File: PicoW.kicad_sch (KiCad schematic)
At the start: 1 part, among them U1 Pico

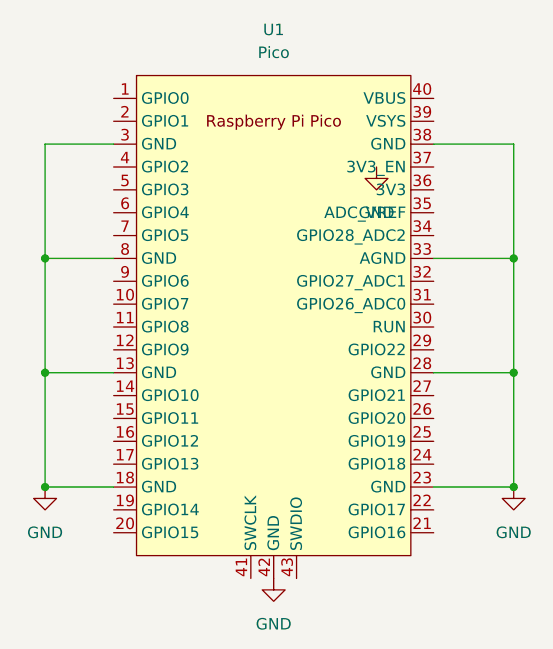
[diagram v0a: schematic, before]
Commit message: Adding pins for Pico
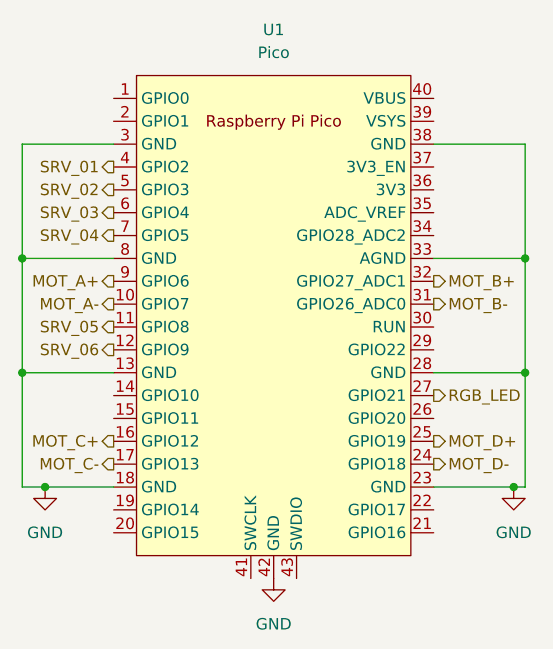
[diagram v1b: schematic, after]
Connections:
- net MOT_A-: now reaches U1.10 (GPIO7)
- net SRV_05: now reaches U1.11 (GPIO8)
- net SRV_06: now reaches U1.12 (GPIO9)
- net MOT_C+: now reaches U1.16 (GPIO12)
- net MOT_C-: now reaches U1.17 (GPIO13)
- net MOT_D-: now reaches U1.24 (GPIO18)
- net MOT_D+: now reaches U1.25 (GPIO19)
- net RGB_LED: now reaches U1.27 (GPIO21)
- net MOT_B-: now reaches U1.31 (GPIO26_ADC0)
- net MOT_B+: now reaches U1.32 (GPIO27_ADC1)
- net SRV_01: now reaches U1.4 (GPIO2)
- net SRV_02: now reaches U1.5 (GPIO3)
- net SRV_03: now reaches U1.6 (GPIO4)
- net SRV_04: now reaches U1.7 (GPIO5)
- net MOT_A+: now reaches U1.9 (GPIO6)
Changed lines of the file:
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@@
 (kicad_sch (version 20230121) (generator eeschema)
   (paper "A4")
+  (junction (at 170.18 97.79) (diameter 0) (color 0 0 0 0)
+  )
+  (junction (at 114.3 85.09) (diameter 0) (color 0 0 0 0)
+  )
+  (junction (at 170.18 85.09) (diameter 0) (color 0 0 0 0)
+  )
   (junction (at 168.91 110.49) (diameter 0) (color 0 0 0 0)
   )
-  (junction (at 168.91 85.09) (diameter 0) (color 0 0 0 0)
-  )
-  (junction (at 116.84 85.09) (diameter 0) (color 0 0 0 0)
-  )
-  (junction (at 168.91 97.79) (diameter 0) (color 0 0 0 0)
+  (junction (at 114.3 97.79) (diameter 0) (color 0 0 0 0)
   )
   (junction (at 116.84 110.49) (diameter 0) (color 0 0 0 0)
   )
-  (junction (at 116.84 97.79) (diameter 0) (color 0 0 0 0)
-  )
-  (wire (pts (xy 168.91 97.79) (xy 168.91 110.49))
+  (wire (pts (xy 170.18 97.79) (xy 170.18 110.49))
     (stroke (width 0) (type default))
   )
-  (wire (pts (xy 168.91 72.39) (xy 168.91 85.09))
+  (wire (pts (xy 114.3 97.79) (xy 124.46 97.79))
     (stroke (width 0) (type default))
   )
-  (wire (pts (xy 160.02 72.39) (xy 168.91 72.39))
+  (wire (pts (xy 170.18 72.39) (xy 170.18 85.09))
     (stroke (width 0) (type default))
   )
-  (wire (pts (xy 160.02 85.09) (xy 168.91 85.09))
+  (wire (pts (xy 114.3 72.39) (xy 114.3 85.09))
     (stroke (width 0) (type default))
   )
-  (wire (pts (xy 116.84 72.39) (xy 116.84 85.09))
+  (wire (pts (xy 160.02 72.39) (xy 170.18 72.39))
     (stroke (width 0) (type default))
   )
@@
     (stroke (width 0) (type default))
   )
-  (wire (pts (xy 116.84 97.79) (xy 124.46 97.79))
+  (wire (pts (xy 114.3 110.49) (xy 116.84 110.49))
     (stroke (width 0) (type default))
   )
-  (wire (pts (xy 160.02 97.79) (xy 168.91 97.79))
+  (wire (pts (xy 160.02 85.09) (xy 170.18 85.09))
+    (stroke (width 0) (type default))
+  )
+  (wire (pts (xy 160.02 97.79) (xy 170.18 97.79))
     (stroke (width 0) (type default))
   )
@@
     (stroke (width 0) (type default))
   )
-  (wire (pts (xy 116.84 97.79) (xy 116.84 110.49))
+  (wire (pts (xy 114.3 97.79) (xy 114.3 110.49))
     (stroke (width 0) (type default))
   )
-  (wire (pts (xy 116.84 85.09) (xy 116.84 97.79))
+  (wire (pts (xy 170.18 110.49) (xy 168.91 110.49))
     (stroke (width 0) (type default))
   )
-  (wire (pts (xy 168.91 85.09) (xy 168.91 97.79))
+  (wire (pts (xy 114.3 85.09) (xy 114.3 97.79))
     (stroke (width 0) (type default))
   )
-  (wire (pts (xy 124.46 72.39) (xy 116.84 72.39))
+  (wire (pts (xy 170.18 85.09) (xy 170.18 97.79))
     (stroke (width 0) (type default))
   )
-  (wire (pts (xy 116.84 85.09) (xy 124.46 85.09))
+  (wire (pts (xy 124.46 72.39) (xy 114.3 72.39))
     (stroke (width 0) (type default))
   )
-  (symbol (lib_id "power:GND") (at 153.67 74.93 0) (unit 1)
-    (in_bom yes) (on_board yes) (dnp no) (fields_autoplaced)
-    (property "Reference" "#PWR016" (at 153.67 81.28 0)
-      (effects (font (size 1.27 1.27)) hide)
-    )
-    (property "Value" "GND" (at 153.67 80.01 0)
-      (effects (font (size 1.27 1.27)))
-    )
-    (property "Footprint" "" (at 153.67 74.93 0)
-      (effects (font (size 1.27 1.27)) hide)
-    )
-    (property "Datasheet" "" (at 153.67 74.93 0)
-      (effects (font (size 1.27 1.27)) hide)
-    )
-    (pin "1")
-    (instances
-      (project "Pico-Skidi"
-        (path "/21865b85-eb74-4d61-a31a-30858d3bc341"
-          (reference "#PWR016") (unit 1)
-        )
-        (path "/21865b85-eb74-4d61-a31a-30858d3bc341/60530e3c-b075-4fd7-83a5-48bc65381cc4"
-          (reference "#PWR010") (unit 1)
-        )
-      )
-    )
+  (wire (pts (xy 114.3 85.09) (xy 124.46 85.09))
+    (stroke (width 0) (type default))
+  )
+  (hierarchical_label "MOT_A+" (shape output) (at 124.46 87.63 180) (fields_autoplaced)
+    (effects (font (size 1.27 1.27)) (justify right))
+  )
+  (hierarchical_label "MOT_A-" (shape output) (at 124.46 90.17 180) (fields_autoplaced)
+    (effects (font (size 1.27 1.27)) (justify right))
+  )
+  (hierarchical_label "SRV_01" (shape output) (at 124.46 74.93 180) (fields_autoplaced)
+    (effects (font (size 1.27 1.27)) (justify right))
+  )
+  (hierarchical_label "SRV_02" (shape output) (at 124.46 77.47 180) (fields_autoplaced)
+    (effects (font (size 1.27 1.27)) (justify right))
+  )
+  (hierarchical_label "SRV_03" (shape output) (at 124.46 80.01 180) (fields_autoplaced)
+    (effects (font (size 1.27 1.27)) (justify right))
+  )
+  (hierarchical_label "MOT_D+" (shape output) (at 160.02 105.41 0) (fields_autoplaced)
+    (effects (font (size 1.27 1.27)) (justify left))
+  )
+  (hierarchical_label "MOT_B-" (shape output) (at 160.02 90.17 0) (fields_autoplaced)
+    (effects (font (size 1.27 1.27)) (justify left))
+  )
+  (hierarchical_label "MOT_C+" (shape output) (at 124.46 105.41 180) (fields_autoplaced)
+    (effects (font (size 1.27 1.27)) (justify right))
+  )
+  (hierarchical_label "MOT_D-" (shape output) (at 160.02 107.95 0) (fields_autoplaced)
+    (effects (font (size 1.27 1.27)) (justify left))
+  )
+  (hierarchical_label "MOT_B+" (shape output) (at 160.02 87.63 0) (fields_autoplaced)
+    (effects (font (size 1.27 1.27)) (justify left))
+  )
+  (hierarchical_label "SRV_04" (shape output) (at 124.46 82.55 180) (fields_autoplaced)
+    (effects (font (size 1.27 1.27)) (justify right))
+  )
+  (hierarchical_label "SRV_06" (shape output) (at 124.46 95.25 180) (fields_autoplaced)
+    (effects (font (size 1.27 1.27)) (justify right))
+  )
+  (hierarchical_label "MOT_C-" (shape output) (at 124.46 107.95 180) (fields_autoplaced)
+    (effects (font (size 1.27 1.27)) (justify right))
+  )
+  (hierarchical_label "SRV_05" (shape output) (at 124.46 92.71 180) (fields_autoplaced)
+    (effects (font (size 1.27 1.27)) (justify right))
+  )
+  (hierarchical_label "RGB_LED" (shape output) (at 160.02 100.33 0) (fields_autoplaced)
+    (effects (font (size 1.27 1.27)) (justify left))
   )
   (symbol (lib_id "MCU_RaspberryPi_and_Boards:Pico") (at 142.24 91.44 0) (unit 1)
@@
         )
         (path "/21865b85-eb74-4d61-a31a-30858d3bc341/60530e3c-b075-4fd7-83a5-48bc65381cc4"
-          (reference "U1") (unit 1)
+          (reference "U?") (unit 1)
         )
       )

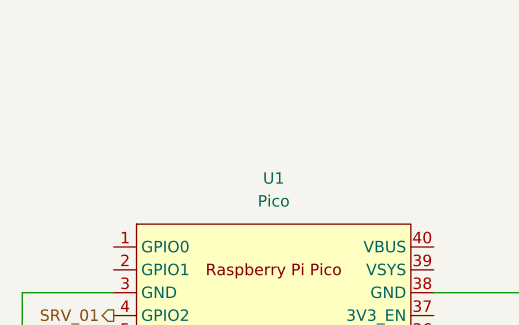
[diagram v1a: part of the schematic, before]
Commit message: Additional sheets in the schematic
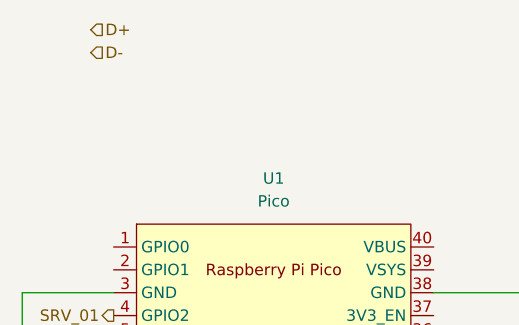
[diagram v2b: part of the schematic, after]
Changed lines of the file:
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@@
+    (effects (font (size 1.27 1.27)) (justify left))
+  )
+  (hierarchical_label "D-" (shape input) (at 121.92 45.72 0) (fields_autoplaced)
     (effects (font (size 1.27 1.27)) (justify left))
   )
@@
     (effects (font (size 1.27 1.27)) (justify right))
   )
+  (hierarchical_label "D+" (shape input) (at 121.92 43.18 0) (fields_autoplaced)
+    (effects (font (size 1.27 1.27)) (justify left))
+  )
   (hierarchical_label "RGB_LED" (shape output) (at 160.02 100.33 0) (fields_autoplaced)

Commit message: Lots of changes
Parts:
- added J7: Conn_01x03, Connector_PinHeader_2.54mm:PinHeader_1x03_P2.54mm_Vertical, symbol Connector_Generic:Conn_01x03
- added J8: Conn_01x04, Connector_PinHeader_2.54mm:PinHeader_1x04_P2.54mm_Vertical, symbol Connector_Generic:Conn_01x04
- U1: footprint RPi_Pico:RPi_Pico_SMD_TH -> MCU_RaspberryPi_and_Boards:RPi_Pico_W_SMD_TH
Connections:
- net GND: now also U1.44 (GND), J7.2 (Pin_2), J8.1 (Pin_1)
- net nFAULT_01: now reaches U1.14 (GPIO10)
- net nFAULT_02: now reaches U1.15 (GPIO11)
- net BUZZER: now reaches U1.19 (GPIO14)
- net SDA: now reaches U1.21 (GPIO16)
- net SDA: now also J8.3 (Pin_3)
- net SCL: now reaches U1.22 (GPIO17)
- net SCL: now also J8.4 (Pin_4)
- net +3.3V: now reaches U1.36 (3V3)
- net +3.3V: now also J8.2 (Pin_2)
- net +5V: now reaches U1.39 (VSYS)
- net VBUS: now reaches U1.40 (VBUS)
- net at U1.41 (SWCLK): now also J7.3 (Pin_3)
- net at U1.43 (SWDIO): now also J7.1 (Pin_1)
- new net BOOTSEL: U1.49 (BOOTSEL)
- new net USB_D+: U1.45 (D+)
- new net USB_D-: U1.46 (D-)
- no-connect marks 0 -> 9

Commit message: syncing
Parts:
- U1: footprint MCU_RaspberryPi_and_Boards:RPi_Pico_W_SMD_TH -> MCU_RaspberryPi_and_Boards:RPi_Pico_W_SMD
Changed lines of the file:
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@@
   (symbol (lib_id "power:+5V") (at 171.45 69.85 0) (unit 1)
     (in_bom yes) (on_board yes) (dnp no) (fields_autoplaced)
-    (property "Reference" "#PWR030" (at 171.45 73.66 0)
+    (property "Reference" "#PWR039" (at 171.45 73.66 0)
       (effects (font (size 1.27 1.27)) hide)
     )
@@
       (project "Pico-Skidi"
         (path "/21865b85-eb74-4d61-a31a-30858d3bc341/60530e3c-b075-4fd7-83a5-48bc65381cc4"
-          (reference "#PWR030") (unit 1)
+          (reference "#PWR039") (unit 1)
         )
       )
@@
   (symbol (lib_id "power:+3.3V") (at 187.96 68.58 0) (unit 1)
     (in_bom yes) (on_board yes) (dnp no) (fields_autoplaced)
-    (property "Reference" "#PWR031" (at 187.96 72.39 0)
+    (property "Reference" "#PWR040" (at 187.96 72.39 0)
       (effects (font (size 1.27 1.27)) hide)
     )
@@
       (project "Pico-Skidi"
         (path "/21865b85-eb74-4d61-a31a-30858d3bc341/60530e3c-b075-4fd7-83a5-48bc65381cc4"
-          (reference "#PWR031") (unit 1)
+          (reference "#PWR040") (unit 1)
         )
       )
@@
   (symbol (lib_id "power:VBUS") (at 165.1 67.31 0) (unit 1)
     (in_bom yes) (on_board yes) (dnp no) (fields_autoplaced)
-    (property "Reference" "#PWR027" (at 165.1 71.12 0)
+    (property "Reference" "#PWR036" (at 165.1 71.12 0)
       (effects (font (size 1.27 1.27)) hide)
     )
@@
       (project "Pico-Skidi"
         (path "/21865b85-eb74-4d61-a31a-30858d3bc341/60530e3c-b075-4fd7-83a5-48bc65381cc4"
-          (reference "#PWR027") (unit 1)
+          (reference "#PWR036") (unit 1)
         )
       )
@@
   (symbol (lib_id "power:+3.3V") (at 166.37 78.74 0) (unit 1)
     (in_bom yes) (on_board yes) (dnp no) (fields_autoplaced)
-    (property "Reference" "#PWR028" (at 166.37 82.55 0)
+    (property "Reference" "#PWR037" (at 166.37 82.55 0)
       (effects (font (size 1.27 1.27)) hide)
     )
@@
       (project "Pico-Skidi"
         (path "/21865b85-eb74-4d61-a31a-30858d3bc341/60530e3c-b075-4fd7-83a5-48bc65381cc4"
-          (reference "#PWR028") (unit 1)
+          (reference "#PWR037") (unit 1)
         )
       )
@@
       (effects (font (size 1.27 1.27)))
     )
-    (property "Footprint" "MCU_RaspberryPi_and_Boards:RPi_Pico_W_SMD_TH" (at 142.24 91.44 90)
+    (property "Footprint" "MCU_RaspberryPi_and_Boards:RPi_Pico_W_SMD" (at 142.24 91.44 90)
       (effects (font (size 1.27 1.27)) hide)
     )
@@
         )
         (path "/21865b85-eb74-4d61-a31a-30858d3bc341/60530e3c-b075-4fd7-83a5-48bc65381cc4"
-          (reference "U4") (unit 1)
+          (reference "U5") (unit 1)
         )
       )
@@
   (symbol (lib_id "power:GND") (at 193.04 62.23 0) (unit 1)
     (in_bom yes) (on_board yes) (dnp no) (fields_autoplaced)
-    (property "Reference" "#PWR032" (at 193.04 68.58 0)
+    (property "Reference" "#PWR041" (at 193.04 68.58 0)
       (effects (font (size 1.27 1.27)) hide)
     )
@@
       (project "Pico-Skidi"
         (path "/21865b85-eb74-4d61-a31a-30858d3bc341/60530e3c-b075-4fd7-83a5-48bc65381cc4"
-          (reference "#PWR032") (unit 1)
+          (reference "#PWR041") (unit 1)
         )
       )
@@
         )
         (path "/21865b85-eb74-4d61-a31a-30858d3bc341/60530e3c-b075-4fd7-83a5-48bc65381cc4"
-          (reference "#PWR029") (unit 1)
+          (reference "#PWR038") (unit 1)
         )
       )
@@
   (symbol (lib_id "power:GND") (at 142.24 128.27 0) (unit 1)
     (in_bom yes) (on_board yes) (dnp no) (fields_autoplaced)
-    (property "Reference" "#PWR026" (at 142.24 134.62 0)
+    (property "Reference" "#PWR035" (at 142.24 134.62 0)
       (effects (font (size 1.27 1.27)) hide)
     )
@@
       (project "Pico-Skidi"
         (path "/21865b85-eb74-4d61-a31a-30858d3bc341/60530e3c-b075-4fd7-83a5-48bc65381cc4"
-          (reference "#PWR026") (unit 1)
+          (reference "#PWR035") (unit 1)
         )
       )
@@
         )
         (path "/21865b85-eb74-4d61-a31a-30858d3bc341/60530e3c-b075-4fd7-83a5-48bc65381cc4"
-          (reference "#PWR025") (unit 1)
-        )
-      )
+          (reference "#PWR034") (unit 1)
+        )
+      )
